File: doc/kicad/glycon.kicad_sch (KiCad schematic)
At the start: 20 parts, among them J1 2x20 Header, J2 USB_B, SW1 SW_Push, U0 Z80CPU, U1 628128_DIP32_SSOP32, U2 SST39SF010, U3 74HC32, U4 74HC86, X1 ACO-6.00MHz

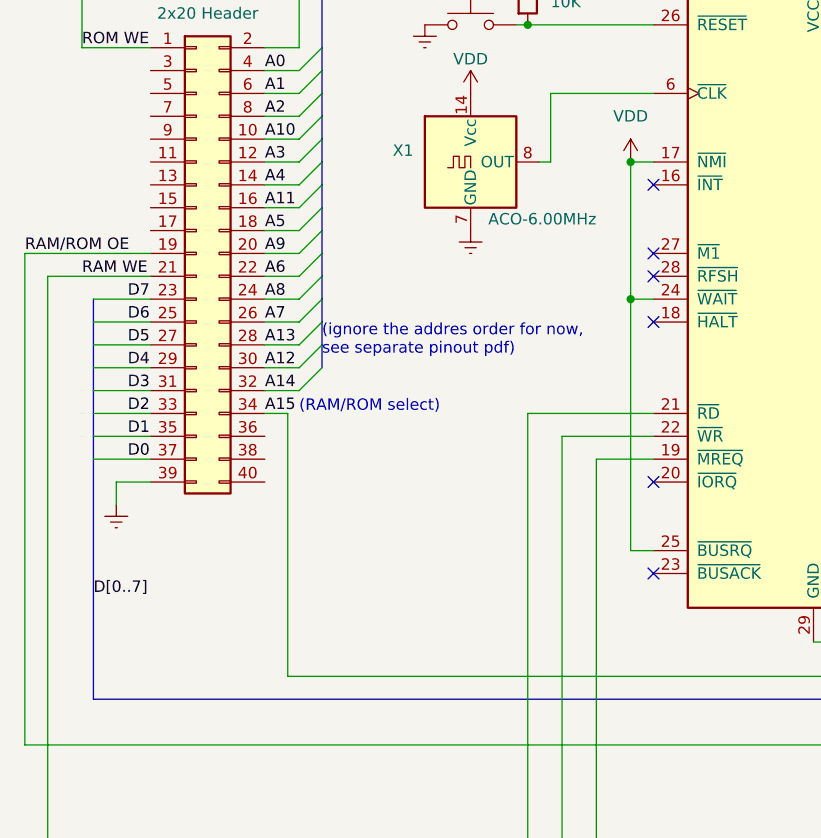
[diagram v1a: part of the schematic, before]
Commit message: connect busack and busrq
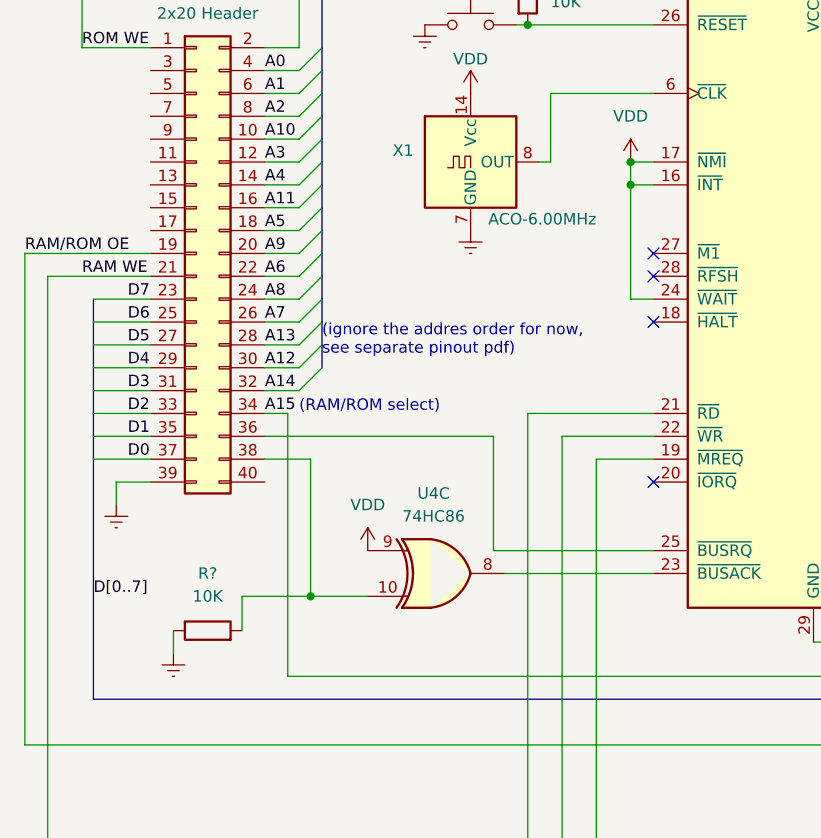
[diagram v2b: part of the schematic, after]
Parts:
- added R?: 10K, Resistor_THT:R_Axial_DIN0204_L3.6mm_D1.6mm_P5.08mm_Horizontal, symbol Device:R
- added unit 3 of U4
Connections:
- net Earth: now also R?.1
- net VDD: now also U0.16 (~{INT}), U4.9; no longer U0.25 (~{BUSRQ})
- net at J1.36 (Pin_36): now also U0.25 (~{BUSRQ})
- net at J1.38 (Pin_38): now also R?.2, U4.10
- net at U0.23 (~{BUSACK}): now also U4.8
- no-connect marks 10 -> 8
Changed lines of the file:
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@@
   (junction (at 234.95 35.56) (diameter 0) (color 0 0 0 0)
   )
+  (junction (at 55.88 109.22) (diameter 0) (color 0 0 0 0)
+  )
   (junction (at 152.4 106.68) (diameter 0) (color 0 0 0 0)
   )
-  (junction (at 91.44 76.2) (diameter 0) (color 0 0 0 0)
-  )
   (junction (at 104.14 140.97) (diameter 0) (color 0 0 0 0)
   )
@@
   )
   (junction (at 91.44 60.96) (diameter 0) (color 0 0 0 0)
+  )
+  (junction (at 91.44 63.5) (diameter 0) (color 0 0 0 0)
   )
   (junction (at 135.89 24.13) (diameter 0) (color 0 0 0 0)
@@
   (no_connect (at 219.71 88.9))
   (no_connect (at 219.71 91.44))
-  (no_connect (at 93.98 63.5))
   (no_connect (at 93.98 73.66))
   (no_connect (at 93.98 71.12))
-  (no_connect (at 93.98 106.68))
   (no_connect (at 93.98 78.74))
   (no_connect (at 93.98 96.52))
@@
     (stroke (width 0) (type default) (color 0 0 0 0))
   )
-  (wire (pts (xy 91.44 76.2) (xy 91.44 104.14))
-    (stroke (width 0) (type default) (color 0 0 0 0))
-  )
   (bus (pts (xy 213.36 48.26) (xy 213.36 45.72))
     (stroke (width 0) (type default) (color 0 0 0 0))
@@
     (stroke (width 0) (type default) (color 0 0 0 0))
   )
+  (wire (pts (xy 55.88 93.98) (xy 55.88 109.22))
+    (stroke (width 0) (type default) (color 0 0 0 0))
+  )
   (wire (pts (xy 250.19 53.34) (xy 254 53.34))
     (stroke (width 0) (type default) (color 0 0 0 0))
@@
     (stroke (width 0) (type default) (color 0 0 0 0))
   )
-  (wire (pts (xy 93.98 104.14) (xy 91.44 104.14))
+  (wire (pts (xy 76.2 104.14) (xy 93.98 104.14))
     (stroke (width 0) (type default) (color 0 0 0 0))
   )
@@
     (stroke (width 0) (type default) (color 0 0 0 0))
   )
+  (wire (pts (xy 76.2 91.44) (xy 50.8 91.44))
+    (stroke (width 0) (type default) (color 0 0 0 0))
+  )
+  (wire (pts (xy 40.64 115.57) (xy 40.64 113.03))
+    (stroke (width 0) (type default) (color 0 0 0 0))
+  )
   (wire (pts (xy 215.9 76.2) (xy 219.71 76.2))
     (stroke (width 0) (type default) (color 0 0 0 0))
@@
     (stroke (width 0) (type default) (color 0 0 0 0))
   )
-  (wire (pts (xy 91.44 60.96) (xy 91.44 76.2))
-    (stroke (width 0) (type default) (color 0 0 0 0))
-  )
   (bus (pts (xy 256.54 66.04) (xy 256.54 120.65))
     (stroke (width 0) (type default) (color 0 0 0 0))
@@
     (stroke (width 0) (type default) (color 0 0 0 0))
   )
+  (wire (pts (xy 91.44 60.96) (xy 91.44 63.5))
+    (stroke (width 0) (type default) (color 0 0 0 0))
+  )
   (wire (pts (xy 50.8 76.2) (xy 54.61 76.2))
     (stroke (width 0) (type default) (color 0 0 0 0))
@@
     (stroke (width 0) (type default) (color 0 0 0 0))
   )
+  (wire (pts (xy 48.26 109.22) (xy 55.88 109.22))
+    (stroke (width 0) (type default) (color 0 0 0 0))
+  )
   (wire (pts (xy 189.23 54.61) (xy 193.04 54.61))
     (stroke (width 0) (type default) (color 0 0 0 0))
@@
     (stroke (width 0) (type default) (color 0 0 0 0))
   )
+  (wire (pts (xy 91.44 63.5) (xy 91.44 76.2))
+    (stroke (width 0) (type default) (color 0 0 0 0))
+  )
   (wire (pts (xy 210.82 96.52) (xy 219.71 96.52))
     (stroke (width 0) (type default) (color 0 0 0 0))
@@
     (stroke (width 0) (type default) (color 0 0 0 0))
   )
+  (wire (pts (xy 77.47 106.68) (xy 93.98 106.68))
+    (stroke (width 0) (type default) (color 0 0 0 0))
+  )
   (bus (pts (xy 31.75 120.65) (xy 135.89 120.65))
     (stroke (width 0) (type default) (color 0 0 0 0))
@@
     (stroke (width 0) (type default) (color 0 0 0 0))
   )
+  (wire (pts (xy 91.44 63.5) (xy 93.98 63.5))
+    (stroke (width 0) (type default) (color 0 0 0 0))
+  )
   (wire (pts (xy 152.4 106.68) (xy 152.4 125.73))
     (stroke (width 0) (type default) (color 0 0 0 0))
   )
+  (wire (pts (xy 55.88 109.22) (xy 62.23 109.22))
+    (stroke (width 0) (type default) (color 0 0 0 0))
+  )
   (wire (pts (xy 160.02 80.01) (xy 163.83 80.01))
     (stroke (width 0) (type default) (color 0 0 0 0))
@@
     (stroke (width 0) (type default) (color 0 0 0 0))
   )
+  (wire (pts (xy 50.8 93.98) (xy 55.88 93.98))
+    (stroke (width 0) (type default) (color 0 0 0 0))
+  )
   (wire (pts (xy 34.29 96.52) (xy 34.29 99.06))
     (stroke (width 0) (type default) (color 0 0 0 0))
@@
     (stroke (width 0) (type default) (color 0 0 0 0))
   )
+  (wire (pts (xy 76.2 104.14) (xy 76.2 91.44))
+    (stroke (width 0) (type default) (color 0 0 0 0))
+  )
   (wire (pts (xy 21.59 191.77) (xy 21.59 185.42))
     (stroke (width 0) (type default) (color 0 0 0 0))
@@
   )
   (bus (pts (xy 135.89 68.58) (xy 135.89 66.04))
+    (stroke (width 0) (type default) (color 0 0 0 0))
+  )
+  (wire (pts (xy 48.26 113.03) (xy 48.26 109.22))
     (stroke (width 0) (type default) (color 0 0 0 0))
   )
@@
     (pin "1")
     (pin "2")
+  )
+  (symbol (lib_id "power:Earth") (at 40.64 115.57 0) (unit 1)
+    (in_bom yes) (on_board yes) (fields_autoplaced)
+    (property "Reference" "#PWR?" (id 0) (at 40.64 121.92 0)
+      (effects (font (size 1.27 1.27)) hide)
+    )
+    (property "Value" "Earth" (id 1) (at 40.64 119.38 0)
+      (effects (font (size 1.27 1.27)) hide)
+    )
+    (property "Footprint" "" (id 2) (at 40.64 115.57 0)
+      (effects (font (size 1.27 1.27)) hide)
+    )
+    (property "Datasheet" "~" (id 3) (at 40.64 115.57 0)
+      (effects (font (size 1.27 1.27)) hide)
+    )
+    (pin "1")
+  )
+  (symbol (lib_id "Device:R") (at 44.45 113.03 90) (unit 1)
+    (in_bom yes) (on_board yes) (fields_autoplaced)
+    (property "Reference" "R?" (id 0) (at 44.45 106.68 90))
+    (property "Value" "10K" (id 1) (at 44.45 109.22 90))
+    (property "Footprint" "Resistor_THT:R_Axial_DIN0204_L3.6mm_D1.6mm_P5.08mm_Horizontal" (id 2) (at 44.45 114.808 90)
+      (effects (font (size 1.27 1.27)) hide)
+    )
+    (property "Datasheet" "~" (id 3) (at 44.45 113.03 0)
+      (effects (font (size 1.27 1.27)) hide)
+    )
+    (pin "1")
+    (pin "2")
+  )
+  (symbol (lib_id "power:VDD") (at 62.23 104.14 0) (unit 1)
+    (in_bom yes) (on_board yes) (fields_autoplaced)
+    (property "Reference" "#PWR?" (id 0) (at 62.23 107.95 0)
+      (effects (font (size 1.27 1.27)) hide)
+    )
+    (property "Value" "VDD" (id 1) (at 62.23 99.06 0))
+    (property "Footprint" "" (id 2) (at 62.23 104.14 0)
+      (effects (font (size 1.27 1.27)) hide)
+    )
+    (property "Datasheet" "" (id 3) (at 62.23 104.14 0)
+      (effects (font (size 1.27 1.27)) hide)
+    )
+    (pin "1")
   )
   (symbol (lib_id "power:Earth") (at 215.9 83.82 0) (unit 1)
@@
     (pin "1")
   )
+  (symbol (lib_id "74xx:74HC86") (at 69.85 106.68 0) (unit 3)
+    (in_bom yes) (on_board yes) (fields_autoplaced)
+    (property "Reference" "U4" (id 0) (at 69.5452 97.79 0))
+    (property "Value" "74HC86" (id 1) (at 69.5452 100.33 0))
+    (property "Footprint" "" (id 2) (at 69.85 106.68 0)
+      (effects (font (size 1.27 1.27)) hide)
+    )
+    (property "Datasheet" "http://www.ti.com/lit/gpn/sn74HC86" (id 3) (at 69.85 106.68 0)
+      (effects (font (size 1.27 1.27)) hide)
+    )
+    (pin "10")
+    (pin "8")
+    (pin "9")
+  )
   (symbol (lib_id "Device:C") (at 151.13 72.39 0) (unit 1)
     (in_bom yes) (on_board yes)
@@
       (reference "#PWR0122") (unit 1) (value "Earth") (footprint "")
     )
+    (path "/0f9726cd-e7a7-48ba-a8a8-b999a75e9200"
+      (reference "#PWR?") (unit 1) (value "Earth") (footprint "")
+    )
+    (path "/158912ed-5283-445d-8566-cdff0f6def98"
+      (reference "#PWR?") (unit 1) (value "VDD") (footprint "")
+    )
     (path "/0efa15df-f1b5-4b7e-8367-a71722e36425"
       (reference "C1") (unit 1) (value "100nF") (footprint "Capacitor_THT:C_Disc_D4.7mm_W2.5mm_P5.00mm")
@@
       (reference "R8") (unit 1) (value "10K") (footprint "Resistor_THT:R_Axial_DIN0204_L3.6mm_D1.6mm_P5.08mm_Horizontal")
     )
+    (path "/13d18af2-1683-4672-bc69-cd47930e9e72"
+      (reference "R?") (unit 1) (value "10K") (footprint "Resistor_THT:R_Axial_DIN0204_L3.6mm_D1.6mm_P5.08mm_Horizontal")
+    )
     (path "/fd3d9773-922e-41cc-b486-19ed8a75f40a"
       (reference "SW1") (unit 1) (value "SW_Push") (footprint "Button_Switch_THT:SW_PUSH_6mm")
@@
       (reference "U4") (unit 2) (value "74HC86") (footprint "")
     )
+    (path "/79e16b3f-0fca-4cd9-9855-aada716213b9"
+      (reference "U4") (unit 3) (value "74HC86") (footprint "")
+    )
     (path "/17782648-7a81-41fd-940c-d4cec184267b"

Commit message: minor schematic updates
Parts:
- U4: footprint (none) -> Package_DIP:DIP-14_W7.62mm_Socket
- gave numbers to parts that had none: 1
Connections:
- net at R4.1, U0.19 (~{MREQ}), U3.1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: now also R3.1, U0.22 (~{WR}), U3.13
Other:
- moved on the sheet: R2, R3, R4, U3C, U3D
